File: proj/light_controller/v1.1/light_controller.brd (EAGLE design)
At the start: 127 x 127 mm, 119 parts, among them J1 0022232051, J2 RJ12, J3 RJ12, J4 1377G2, J5 RJ12, J6 RJ12, U1 RCD-24-0.70/VREF, U10 ADM2481BRWZ-RL7, U11 PHOTONH, U12 TLV70433DBVR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

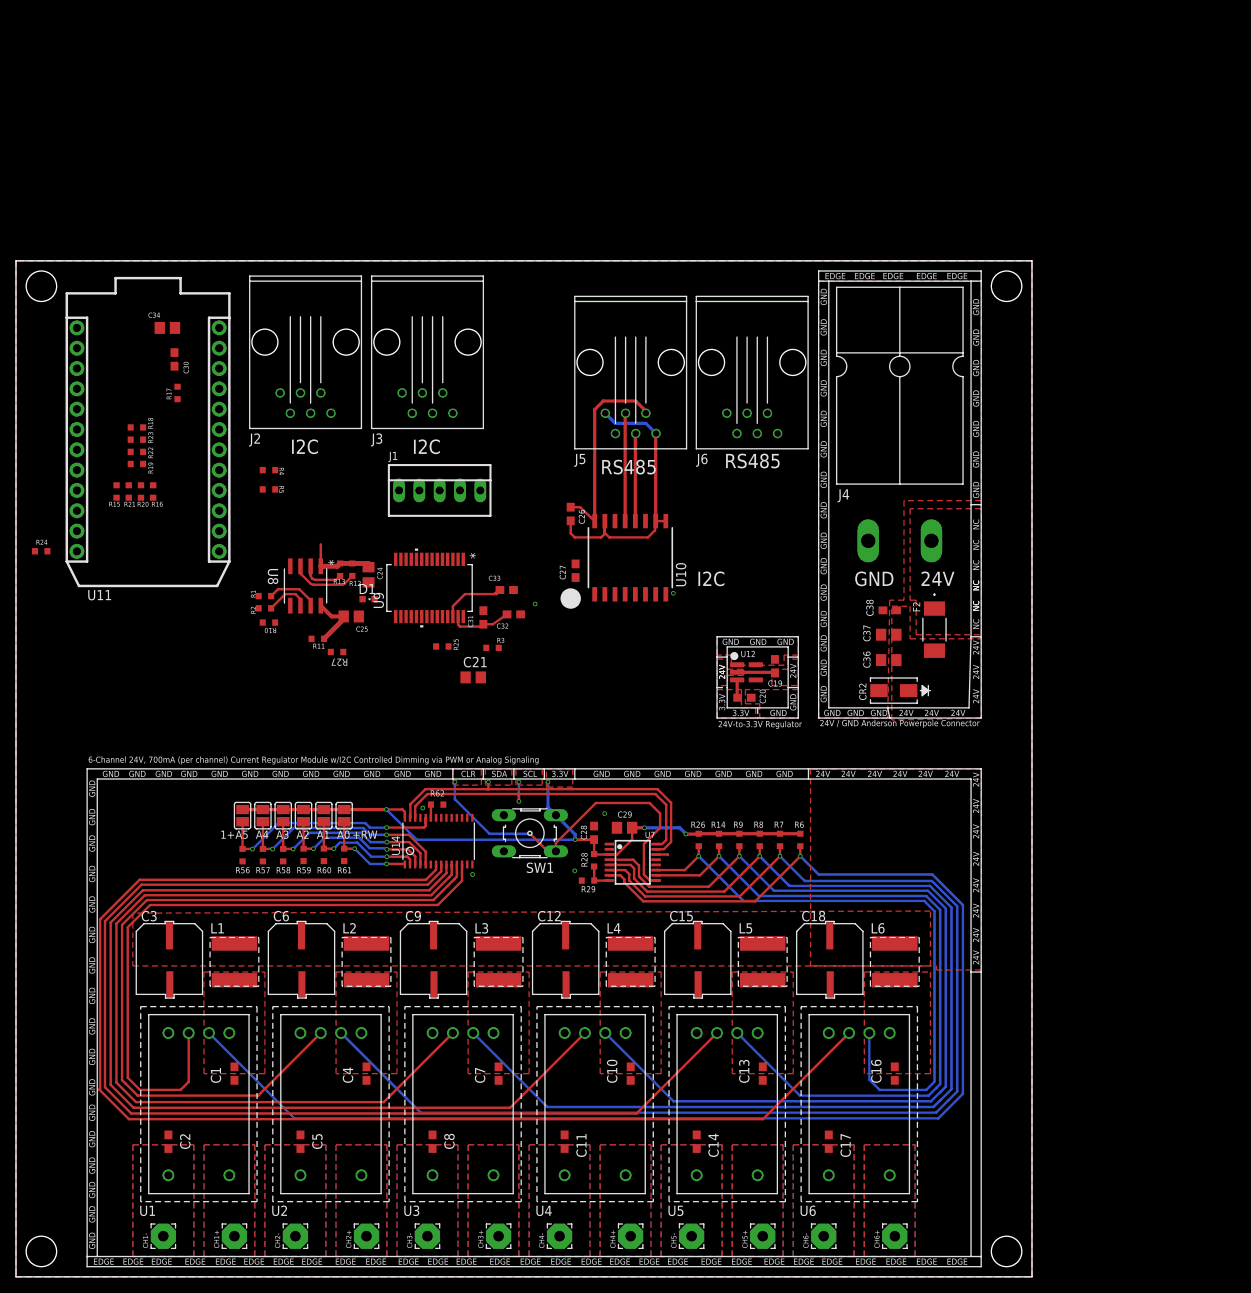
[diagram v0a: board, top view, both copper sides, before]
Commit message: explored new modularity concept for light controller
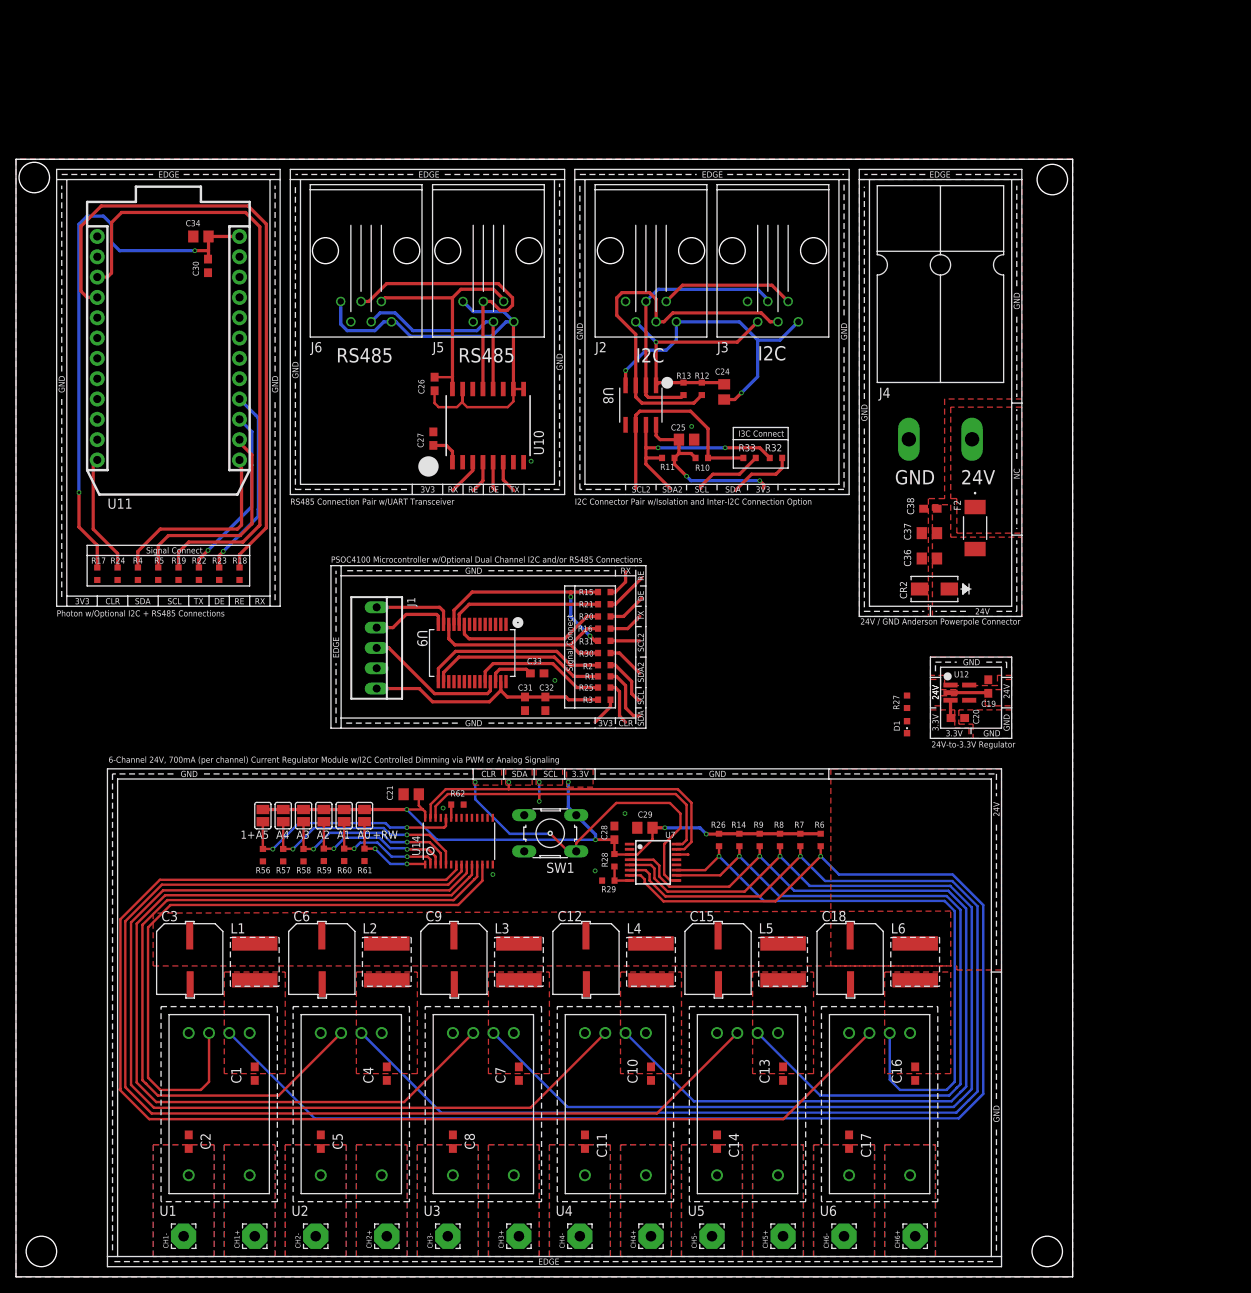
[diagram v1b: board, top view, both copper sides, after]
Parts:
- added R30, R31, R32, R33: 0 OHM, openag-resistors:RC0603N
- moved FRAME1 129.0 mm to (1.91, 6.35), turned to 90 degrees
- moved R27 71.5 mm to (111.4, 71.9), turned to 90 degrees
- moved D1 69.2 mm to (111.4, 68.7), turned to 180 degrees
- moved R15 62.2 mm to (73.5, 85.6), turned to 0 degrees
- moved R21 61.1 mm to (73.5, 84.1), turned to 0 degrees
- moved R20 60.0 mm to (73.5, 82.5), turned to 0 degrees
- moved R16 58.9 mm to (73.5, 81.0), turned to 0 degrees
- moved R10 57.9 mm to (85.7, 102.4), turned to 180 degrees
- moved J6 50.2 mm to (43.8, 128.3)
- moved C24 50.0 mm to (88.5, 110.6)
- moved R11 49.3 mm to (81.5, 102.4)
- moved R12 49.2 mm to (85.7, 111.0)
- moved R13 48.5 mm to (83.4, 111.0)
- moved U8 47.6 mm to (78.1, 109.0)
- moved C25 47.4 mm to (83.8, 104.6)
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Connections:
- net I2C_SCL renamed SCL1
- net I2C_SDA renamed SDA1
- removed net SCB1_RX[0]: R15.1, U9.11
- removed net SCB1_TX[0]: R16.1, U9.12
- new net SCB1_RX[0]_SCL[0]: R15.1, R31.1, U9.11
- new net SCB1_TX[0]_SDA[0]: R16.1, R30.1, U9.12
- new net SCL2: R10.1, R31.2, R33.1, U8.6
- new net SDA2: R11.1, R30.2, R32.1, U8.7
- net PHOTON_D2: now also R22.1; no longer R23.1
- net PHOTON_D3: now also R23.1; no longer R22.1
- net SCL: now also R33.2; no longer R10.1, U8.6
- net SDA: now also R32.2; no longer R11.1, U8.7
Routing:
- net PHOTON_RX: track 0.00 -> 80.0 mm
- net PHOTON_TX: track 0.10 -> 78.9 mm
- net N$8: track 0.00 -> 70.3 mm, vias 0 -> 2
- net I2C_GND: track 0.00 -> 39.1 mm, vias 0 -> 2
- net SCL1: track 8.53 -> 47.1 mm
- net SDA2: track 0.00 -> 32.0 mm, vias 0 -> 2
- net SCL2: track 0.00 -> 31.0 mm
- net SCB1_RX[0]_SCL[0]: track 0.00 -> 28.5 mm, vias 0 -> 2
- net SDA1: track 5.25 -> 33.0 mm
- net PHOTON_SCL: track 0.00 -> 26.7 mm
- net SCB1_TX[0]_SDA[0]: track 0.00 -> 25.4 mm
- net +3V3: track 94.8 -> 120.0 mm, vias 5 -> 7
- net PHOTON_SDA: track 0.00 -> 24.6 mm
- net 485_GND: track 36.9 -> 61.1 mm
- net PHOTON_D3: track 0.00 -> 24.1 mm, vias 0 -> 1
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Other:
- board size 127 x 127 mm -> 132.1 x 139.7 mm
- board text added: "3V3"
- board text added: "DE"
- board text added: "I2C Connector Pair w/Isolation and Inter-I2C Connection Option"
- board text added: "I3C Connect"
- board text added: "PSOC4100 Microcontroller w/Optional Dual Channel I2C and/or RS485 Connections"
- board text added: "Photon w/Optional I2C + RS485 Connections"
- board text added: "RE"
- board text added: "RS485 Connection Pair w/UART Transceiver"
- board text added: "RX"
- board text added: "SCL2"
- board text added: "SDA2"
- board text added: "Signal Connect"
- board text added: "TX"

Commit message: majority of design changes done for light controller v1.1
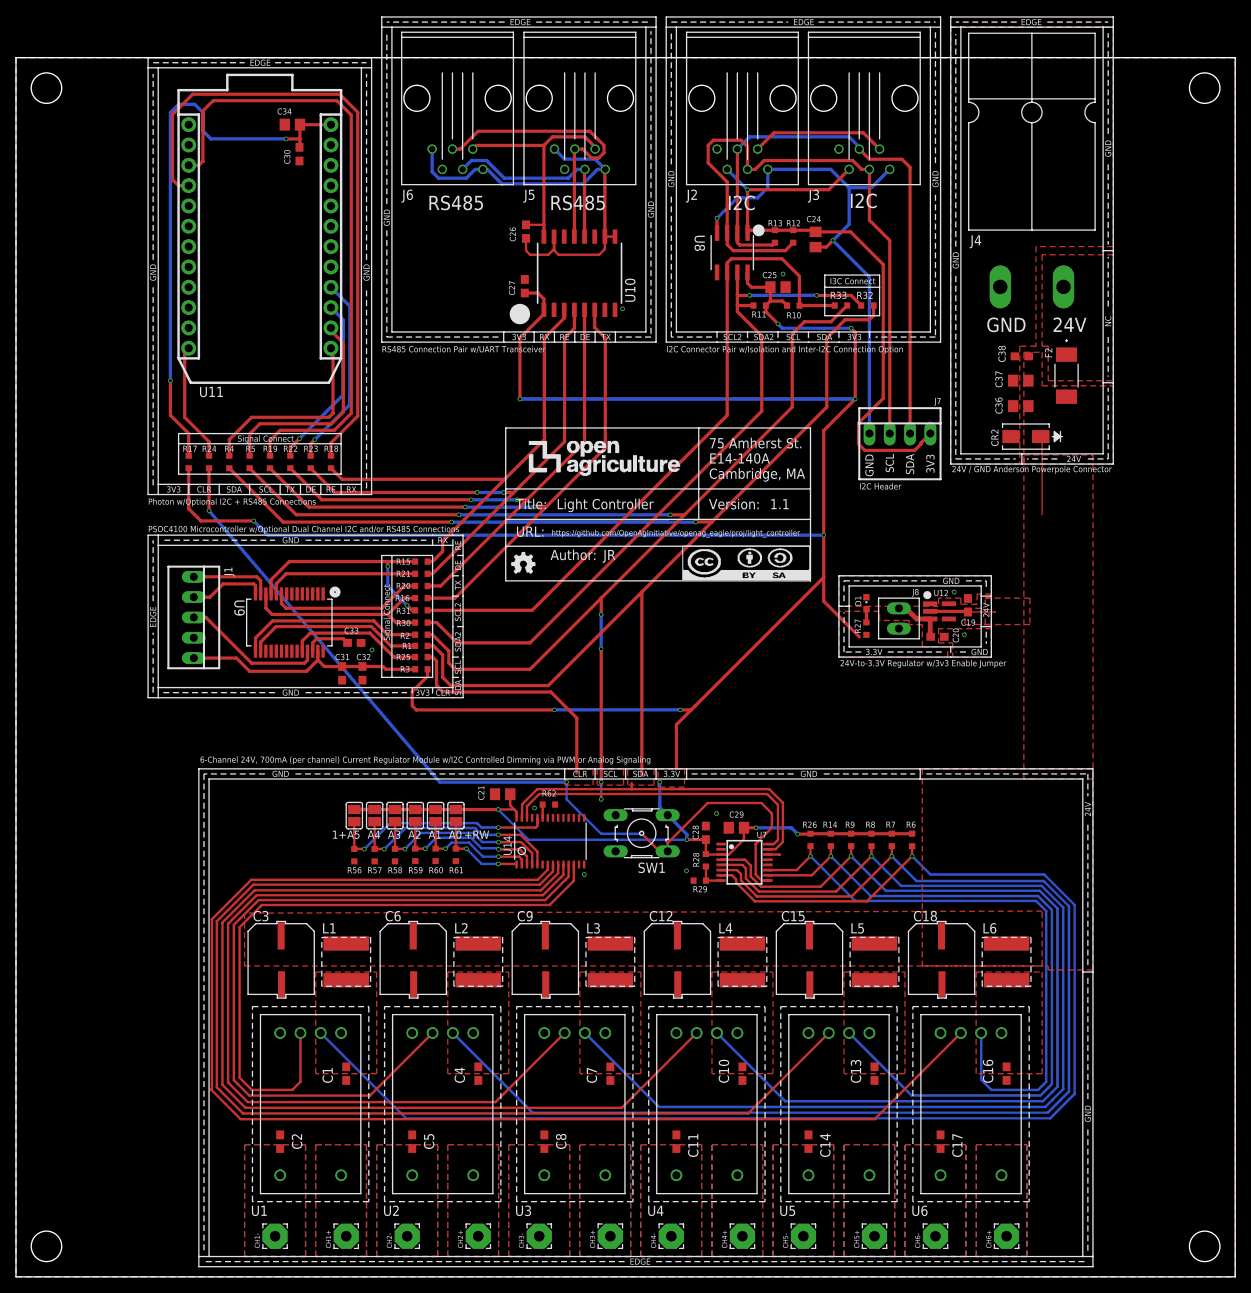
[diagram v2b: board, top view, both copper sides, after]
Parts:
- added J7: OPENAG-I2C-HEADER, openag-connectors:OPENAG-I2C-HEADER
- added J8: JUMPER, openag-connectors:1X2-100-MIL-HEADER
- added U$1, U$2, U$3, U$4: (no value), openag-frames:OPENAG-CORNER-MOUNTING-HOLE
- J2, J3, J5, J6: value RJ12 -> A-2004-1-4-LP-N-R
- SW1: value (none) -> BF3-1020
- moved FRAME1 100.1 mm to (61.2, 87.0), flipped to the top, turned to 0 degrees
- moved U9 23.2 mm to (34.2, 81.8)
- moved C31 23.2 mm to (40.8, 75.4)
- moved C32 23.2 mm to (43.3, 75.4)
- moved C33 23.2 mm to (42.3, 79.2)
- moved J1 23.2 mm to (22.2, 82.4)
- moved R1 23.2 mm to (50.7, 78.9)
- moved R15 23.2 mm to (50.7, 89.4)
- moved R16 23.2 mm to (50.7, 84.8)
- moved R2 23.2 mm to (50.7, 80.3)
- moved R20 23.2 mm to (50.7, 86.4)
- moved R21 23.2 mm to (50.7, 87.9)
- moved R25 23.2 mm to (50.7, 77.5)
- moved R3 23.2 mm to (50.7, 75.9)
- moved R30 23.2 mm to (50.7, 81.8)
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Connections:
- net +3V3: now also J8.2
- net I2C_3V3: now also J7.3V3
- net I2C_GND: now also J7.GND
- net REG_3V3: now also J8.1
- net SCL1: now also J7.SCL
- net SDA1: now also J7.SDA
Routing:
- net +3V3: track 120.0 -> 369.6 mm, vias 7 -> 13
- net SDA: track 59.5 -> 214.6 mm, vias 1 -> 2
- net SCL: track 58.2 -> 201.8 mm, vias 2 -> 6
- net DAC_!CLR!: track 50.3 -> 141.0 mm, vias 2 -> 3
- net UART_TX: track 8.44 -> 84.4 mm, vias 0 -> 2
- net UART_DE: track 8.59 -> 74.9 mm, vias 0 -> 2
- net SDA2: track 32.0 -> 91.5 mm
- net UART_!RE!: track 9.39 -> 67.7 mm, vias 0 -> 2
- net SCL2: track 31.0 -> 84.8 mm
- net UART_RX: track 8.32 -> 61.3 mm
- net I2C_3V3: track 31.5 -> 75.6 mm
- net SDA1: track 33.0 -> 73.9 mm
- net SCL1: track 47.1 -> 81.1 mm
- net I2C_GND: track 39.1 -> 65.2 mm
- net +24V: track 4.89 -> 18.3 mm
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- removed copper zone on layer 1, net REG_3V3
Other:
- board size 132.1 x 139.7 mm -> 152.4 x 152.4 mm
- board text added: "24V-to-3.3V Regulator w/3v3 Enable Jumper"
- board text added: "I2C Header"
- board text removed: "24V-to-3.3V Regulator"

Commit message: sent light controller v1.1 to fab house
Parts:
- J2, J3: value A-2004-1-4-LP-N-R -> OPENAG-I2C-RJ12; device openag-connectors:RJ12 -> openag-connectors:OPENAG-I2C-RJ12
- J5, J6: value A-2004-1-4-LP-N-R -> OPENAG-RS485-RJ12; device openag-connectors:RJ12 -> openag-connectors:OPENAG-RS485-RJ12
- moved R57 2.54 mm to (42.3, 52.7)
- moved SJ_A4 2.54 mm to (42.3, 57.7)
- moved R56 2.54 mm to (39.8, 52.7)
- moved R58 2.54 mm to (44.8, 52.7)
- moved R59 2.54 mm to (47.4, 52.7)
- moved R60 2.54 mm to (49.9, 52.7)
- moved R61 2.54 mm to (52.5, 52.7)
- moved SJ_A0 2.54 mm to (52.5, 57.7)
- moved SJ_A1 2.54 mm to (49.9, 57.7)
- moved SJ_A2 2.54 mm to (47.4, 57.7)
- moved SJ_A3 2.54 mm to (44.8, 57.7)
- moved SJ_A5 2.54 mm to (39.8, 57.7)
- moved C29 0.92 mm to (90.9, 56.4)
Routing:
- net A4: track 27.8 -> 30.4 mm
- net A5: track 30.0 -> 32.6 mm
- net A3: track 23.9 -> 26.4 mm
- net A2: track 19.9 -> 22.4 mm
- net A0: track 11.8 -> 14.3 mm
- net A1: track 16.0 -> 18.5 mm
- net +3V3: track 369.6 -> 372.0 mm
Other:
- board text added: "ADM2481: RS485 Isolator w/UART Transceiver"
- board text added: "DAC5578: 8-Channel, 8-bit I2C DAC"
- board text added: "ISO1540: I2C Isolator"
- board text added: "Light Controller v1.1: Controls 6 channels of 24V, 700mA for LED strings that can be interfaced via i2c, rs485, and/or wifi."
- board text added: "PCA9685 Address Set"
- board text added: "PCA9685: 16-Channel, 12-bit FM+ I2C PWM Driver"
- board text added: "PSOC4100: 32-bit 24MHz ARM-M0 Microcontroller"
- board text added: "Photon Microcontroller w/Optional I2C + RS485 Connections"
- board text added: "Photon: 32-bit 120MHz ARM-M3 Microcontroller w/wifi"
- board text added: "Programming Header"
- board text removed: "Photon w/Optional I2C + RS485 Connections"
